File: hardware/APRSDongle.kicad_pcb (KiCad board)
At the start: 2 copper layers, 34 parts, among them IC1 DRA818, J1 SMA, P1 VIN, P2 GPS, P3 PC_CON, P4 CONN_8, P5 SWD, U1 AP7363, U2 KL05

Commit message: finished routing
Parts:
- D1: value LED -> PWRSTAT
- moved DRAC1 90.5 mm to (388.0, 210.0)
- moved C5 74.3 mm to (352.0, 232.0)
- moved DRAPOW1 67.5 mm to (382.0, 210.0)
- moved HLSEL1 65.8 mm to (376.0, 210.0), turned to 180 degrees
- moved R3 60.8 mm to (349.2, 230.2), turned to 270 degrees
- moved C8 59.8 mm to (365.5, 210.0), turned to 180 degrees
- moved C2 58.1 mm to (352.0, 227.5), turned to 270 degrees
- moved C1 50.0 mm to (346.0, 228.5)
- moved DACEN1 47.0 mm to (354.5, 236.2)
- moved R1 38.5 mm to (340.5, 230.5)
- moved P5 24.6 mm to (341.0, 238.5), turned to 90 degrees
- moved P3 24.4 mm to (350.0, 240.5), turned to 180 degrees
- moved P2 23.8 mm to (350.0, 243.5), turned to 180 degrees
- moved STAT1 21.2 mm to (346.5, 232.5), turned to 180 degrees
- moved STAT0 16.0 mm to (346.5, 235.0), turned to 180 degrees
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- renumbered JP2 to DACEN1, C6 to DRAC1, JP3 to DRAPOW1, JP1 to HLSEL1, D3 to STAT0, D4 to STAT1
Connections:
- P3 pad 3: /DAC -> /GPS2MC
- P3 pad 4: /GPS2MC -> /DAC
- U1 pad 1: GND -> N-000001
- U1 pad 2: (no net) -> GND
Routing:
- net GND: track 10.5 -> 157.5 mm, vias 0 -> 4
- net +3.3V: track 0.00 -> 111.3 mm, vias 0 -> 7
- net /GPS2MC: track 0.00 -> 44.2 mm, vias 0 -> 2
- net /MCU2PD: track 0.00 -> 39.8 mm
- net /MCU2PTT: track 0.00 -> 32.5 mm
- net /MC2DRA: track 0.00 -> 32.3 mm, vias 0 -> 2
- net /DAC: track 0.00 -> 29.3 mm, vias 0 -> 2
- net /DRA2MC: track 0.00 -> 25.2 mm, vias 0 -> 2
- net /SWD_DIO: track 0.00 -> 22.6 mm, vias 0 -> 1
- net /SWD_CLK: track 0.00 -> 22.0 mm
- net N-000006: track 0.00 -> 20.9 mm
- net /ADC0_6: track 0.00 -> 18.9 mm
- net /PTA6: track 0.00 -> 17.9 mm, vias 0 -> 1
- net /SQ2MC: track 0.00 -> 14.3 mm
- net /PTA7: track 0.00 -> 14.1 mm
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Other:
- board outline added: 56.6 x 39.2 mm
- net class Default: clearance 0.254 -> 0.175
- rule trace_clearance: 0.254 -> 0.175

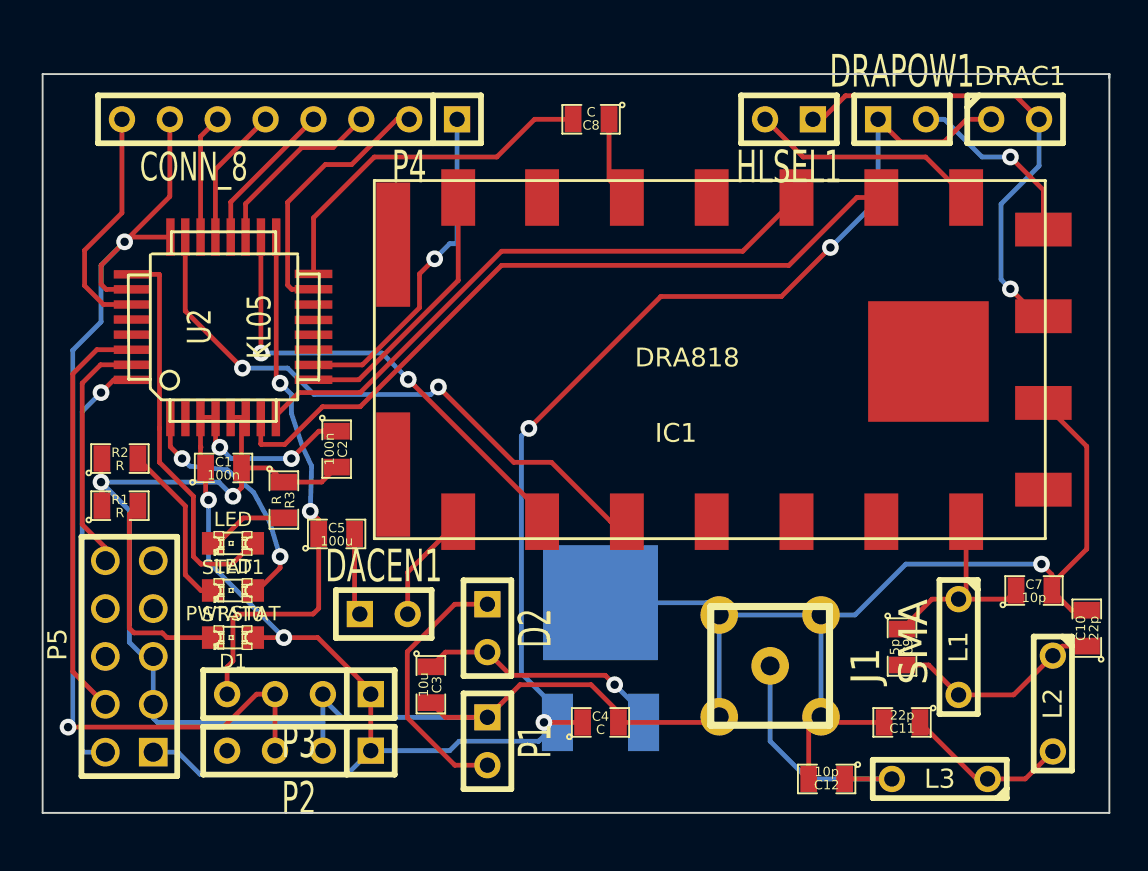
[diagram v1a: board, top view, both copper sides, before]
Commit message: finished routing. Gerber generated.
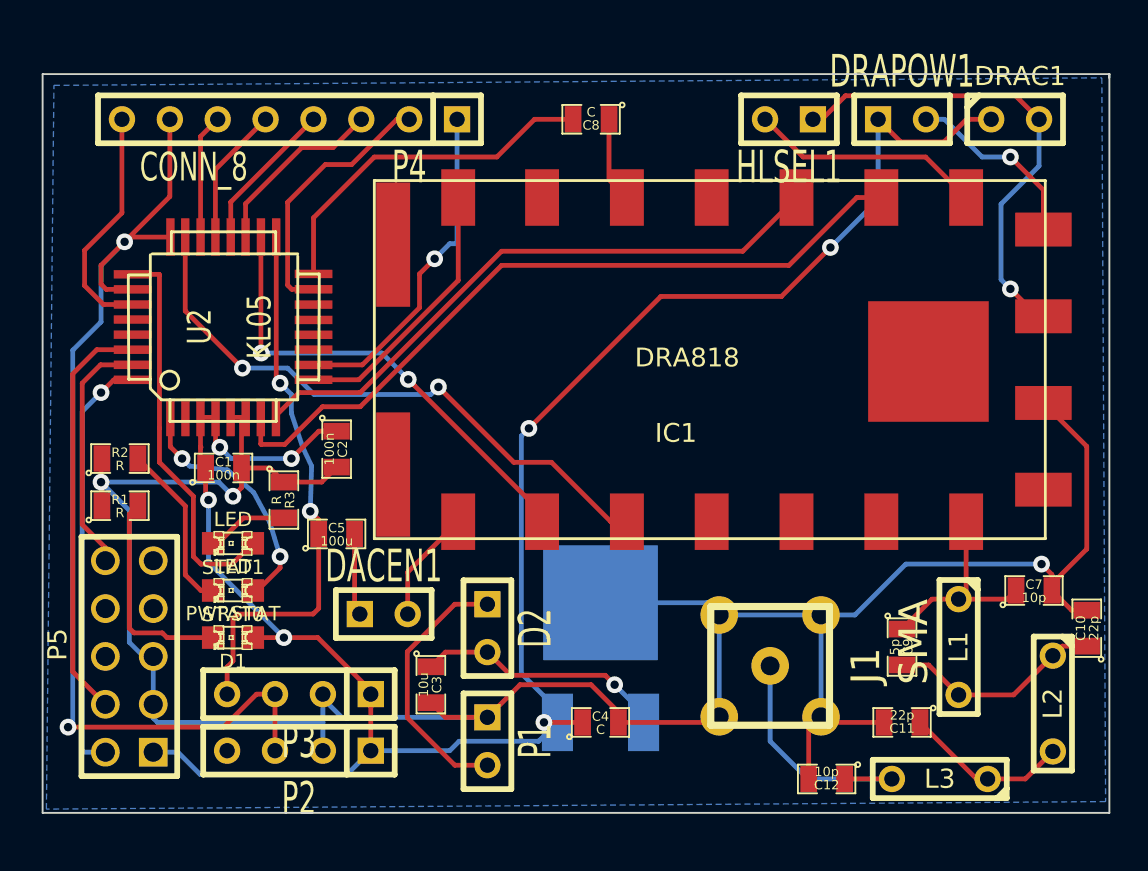
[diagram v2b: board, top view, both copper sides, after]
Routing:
- added copper zone on B.Cu, net GND
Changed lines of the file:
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@@
   (segment (start 338.5 231.5) (end 338.5 224) (width 0.254) (layer F.Cu) (net 20))
   (segment (start 339.73 232.73) (end 338.5 231.5) (width 0.254) (layer F.Cu) (net 20))
-  (segment (start 391.8 236.0475) (end 391 236.0475) (width 0.254) (layer F.Cu) (net 21) (status 400000))
-  (segment (start 391 236.0475) (end 389.9525 235) (width 0.254) (layer F.Cu) (net 21) (status 800000))
+  (segment (start 391.8 236.0475) (end 391 236.0475) (width 0.254) (layer F.Cu) (net 21))
+  (segment (start 391 236.0475) (end 389.9525 235) (width 0.254) (layer F.Cu) (net 21))
   (segment (start 349.2 229.2475) (end 351.205 229.2475) (width 0.254) (layer F.Cu) (net 21))
   (segment (start 351.205 229.2475) (end 352 228.4525) (width 0.254) (layer F.Cu) (net 21))
@@
   (segment (start 352.9525 232) (end 352.9525 235.9725) (width 0.254) (layer F.Cu) (net 24))
   (segment (start 352.9525 235.9725) (end 353.23 236.25) (width 0.254) (layer F.Cu) (net 24))
-  (segment (start 391.8 237.9525) (end 390.5075 237.9525) (width 0.254) (layer F.Cu) (net 25) (status 400000))
-  (segment (start 390.5075 237.9525) (end 390 238.46) (width 0.254) (layer F.Cu) (net 25) (status 800000))
+  (segment (start 391.8 237.9525) (end 390.5075 237.9525) (width 0.254) (layer F.Cu) (net 25))
+  (segment (start 390.5075 237.9525) (end 390 238.46) (width 0.254) (layer F.Cu) (net 25))
   (segment (start 385 240.54) (end 387.92 240.54) (width 0.254) (layer F.Cu) (net 25))
   (segment (start 387.92 240.54) (end 390 238.46) (width 0.254) (layer F.Cu) (net 25))
@@
   (segment (start 376.75 212) (end 383.25 212) (width 0.254) (layer F.Cu) (net 37))
   (segment (start 374.75 210) (end 376.75 212) (width 0.254) (layer F.Cu) (net 37))
+  (zone (net 21) (net_name GND) (layer B.Cu) (hatch edge 0.508)
+    (connect_pads (clearance 0.508))
+    (min_thickness 0.254)
+    (fill (arc_segments 16) (thermal_gap 0.508) (thermal_bridge_width 0.508))
+    (polygon
+      (pts
+        (xy 337 208.2) (xy 392.6 207.8) (xy 392.8 246.2) (xy 336.6 246.6)
+      )
+    )
+  )
 )

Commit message: Finished, pending Johns critique
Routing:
- net GND: track 157.5 -> 168.0 mm, vias 4 -> 6
- net N-0000010: track 13.8 -> 12.7 mm
- net N-000001: track 13.4 -> 14.4 mm
- net N-000007: track 14.1 -> 14.8 mm
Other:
- net class RF added: clearance 0.2, trace_width 0.6, via_dia 0.889, via_drill 0.635
- net class power added: clearance 0.175, trace_width 0.7, via_dia 0.889, via_drill 0.635
- board text added: "APRSDongle AB1TJ"

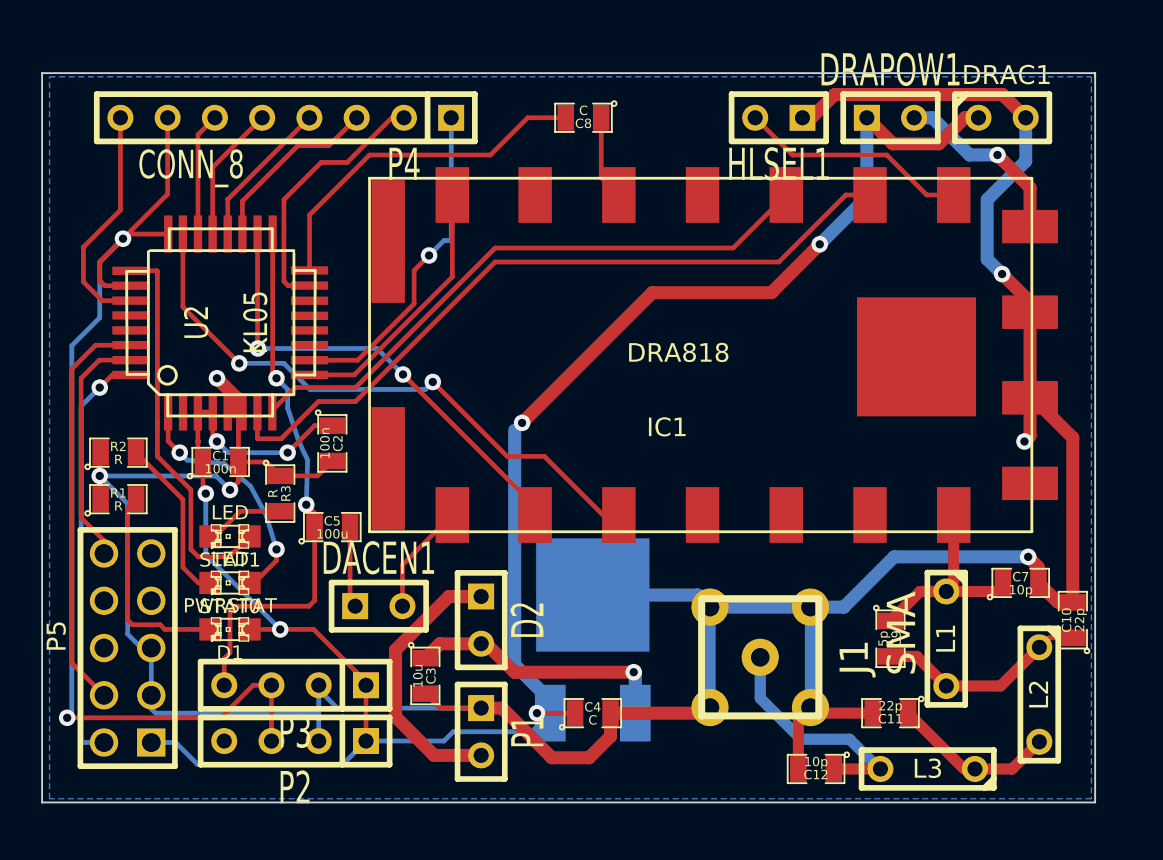
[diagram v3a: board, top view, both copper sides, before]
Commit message: removed lpf, fixed an error
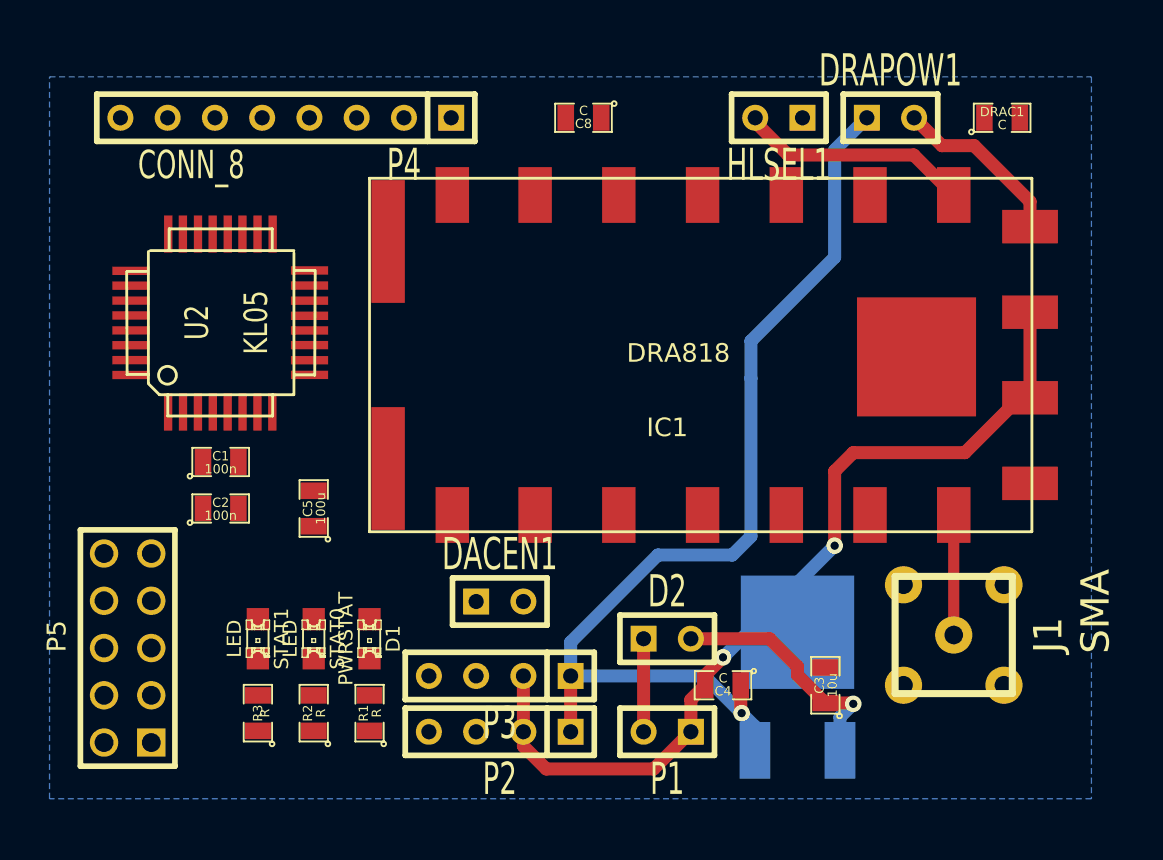
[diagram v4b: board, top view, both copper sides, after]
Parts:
- removed C10, C11: 22p, SM0805
- removed C12, C7: 10p, SM0805
- removed C9: 5p, SM0805
- removed L1: 2Turns, C2
- removed L2, L3: 3Turns, C2
- DRAC1: footprint C1 -> SM0805
- moved C3 21.5 mm to (378.5, 240.5), turned to 90 degrees
- moved R1 17.7 mm to (354.0, 242.0), turned to 90 degrees
- moved R2 17.5 mm to (351.0, 242.0), turned to 90 degrees
- moved R3 11.9 mm to (348.0, 242.0), turned to 90 degrees
- moved U1 11.2 mm to (377.0, 244.0)
- moved P2 11.0 mm to (361.0, 243.0)
- moved P3 11.0 mm to (361.0, 240.0)
- moved J1 10.5 mm to (385.4, 237.8)
- moved D2 10.0 mm to (370.0, 238.0), turned to 0 degrees
- moved P1 10.0 mm to (370.0, 243.0), turned to 180 degrees
- moved D1 7.52 mm to (354.0, 238.0), turned to 270 degrees
- moved C4 7.16 mm to (373.0, 240.5), turned to 180 degrees
- moved C2 6.95 mm to (346.0, 231.0), turned to 0 degrees
- moved DACEN1 6.50 mm to (361.0, 236.0)
- moved STAT1 5.70 mm to (348.0, 238.0), turned to 270 degrees
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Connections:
- IC1 pad 12: N-000003 -> N-0000033
- J1 pad 1: N-0000010 -> N-0000033
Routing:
- net GND: track 168.0 -> 49.6 mm, vias 6 -> 2
- net +3.3V: track 111.5 -> 55.8 mm, vias 7 -> 1
- net /GPS2MC: track 44.2 -> 0.00 mm, vias 2 -> 0
- net /MCU2PD: track 39.8 -> 0.00 mm
- net /MCU2PTT: track 32.5 -> 0.00 mm
- net /MC2DRA: track 32.3 -> 0.00 mm, vias 2 -> 0
- net /DAC: track 29.3 -> 0.00 mm, vias 2 -> 0
- net /DRA2MC: track 25.2 -> 0.00 mm, vias 2 -> 0
- net /SWD_DIO: track 22.6 -> 0.00 mm, vias 1 -> 0
- net /SWD_CLK: track 22.0 -> 0.00 mm
- net N-0000032: track 20.9 -> 0.00 mm
- net /ADC0_6: track 18.9 -> 0.00 mm
- net /PTA6: track 17.9 -> 0.00 mm, vias 1 -> 0
- net /SQ2MC: track 14.3 -> 0.00 mm
- net /PTA7: track 14.1 -> 0.00 mm
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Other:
- board outline removed
- board text removed: "APRSDongle AB1TJ"
